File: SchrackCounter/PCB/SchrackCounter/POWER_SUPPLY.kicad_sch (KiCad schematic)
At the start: 4 parts, among them J1 Conn_01x02_Pin

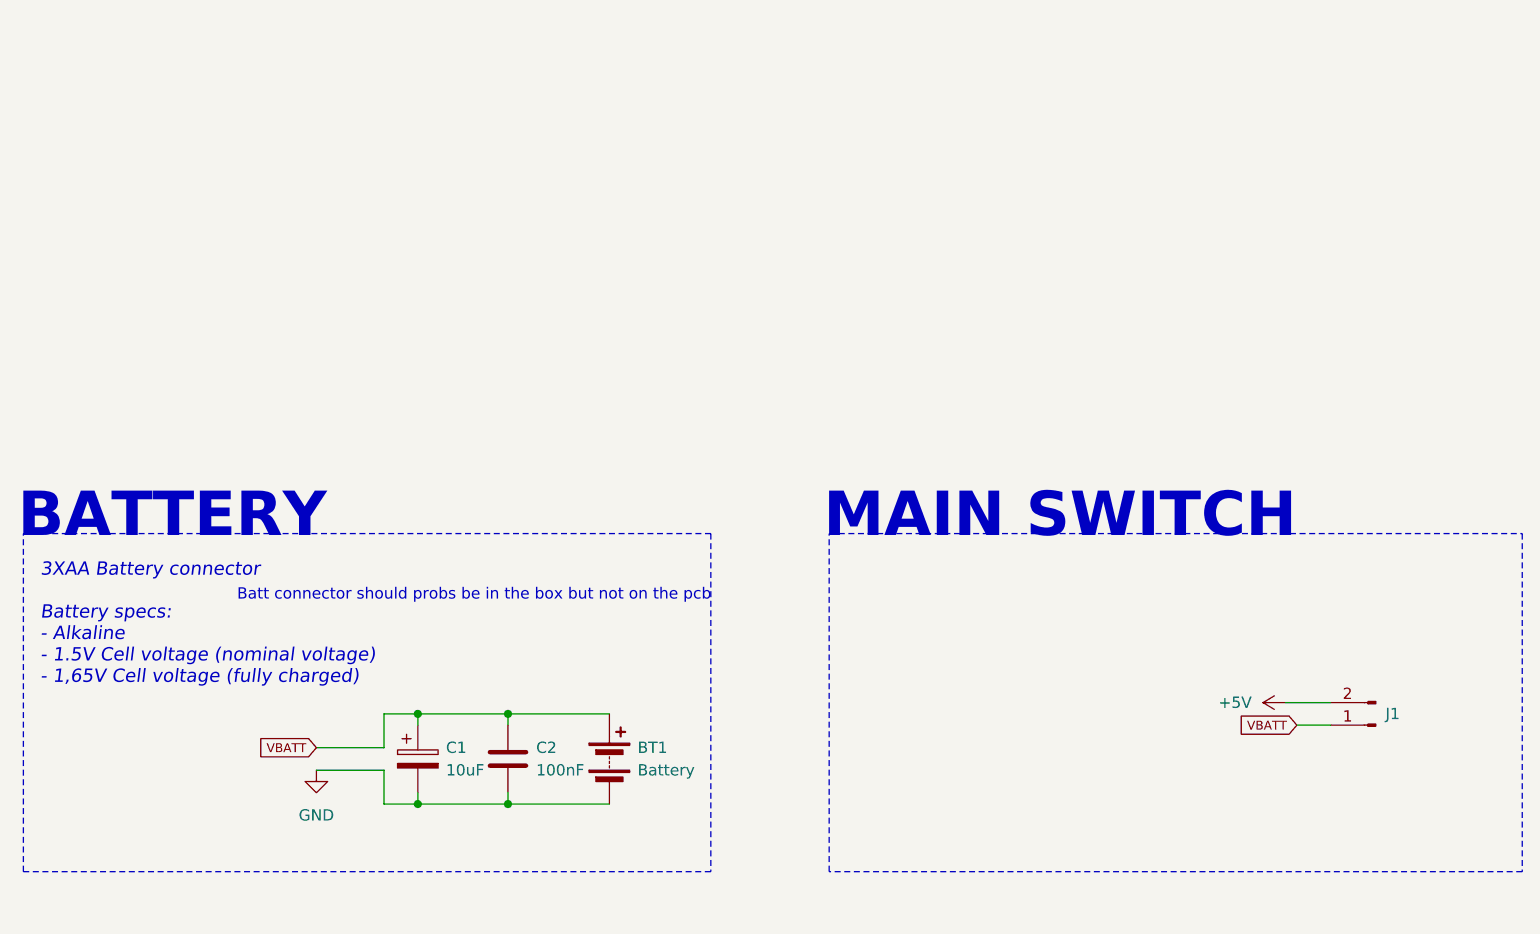
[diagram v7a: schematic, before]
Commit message: Schematic and PCB update
LDO Regulator, and some layout update
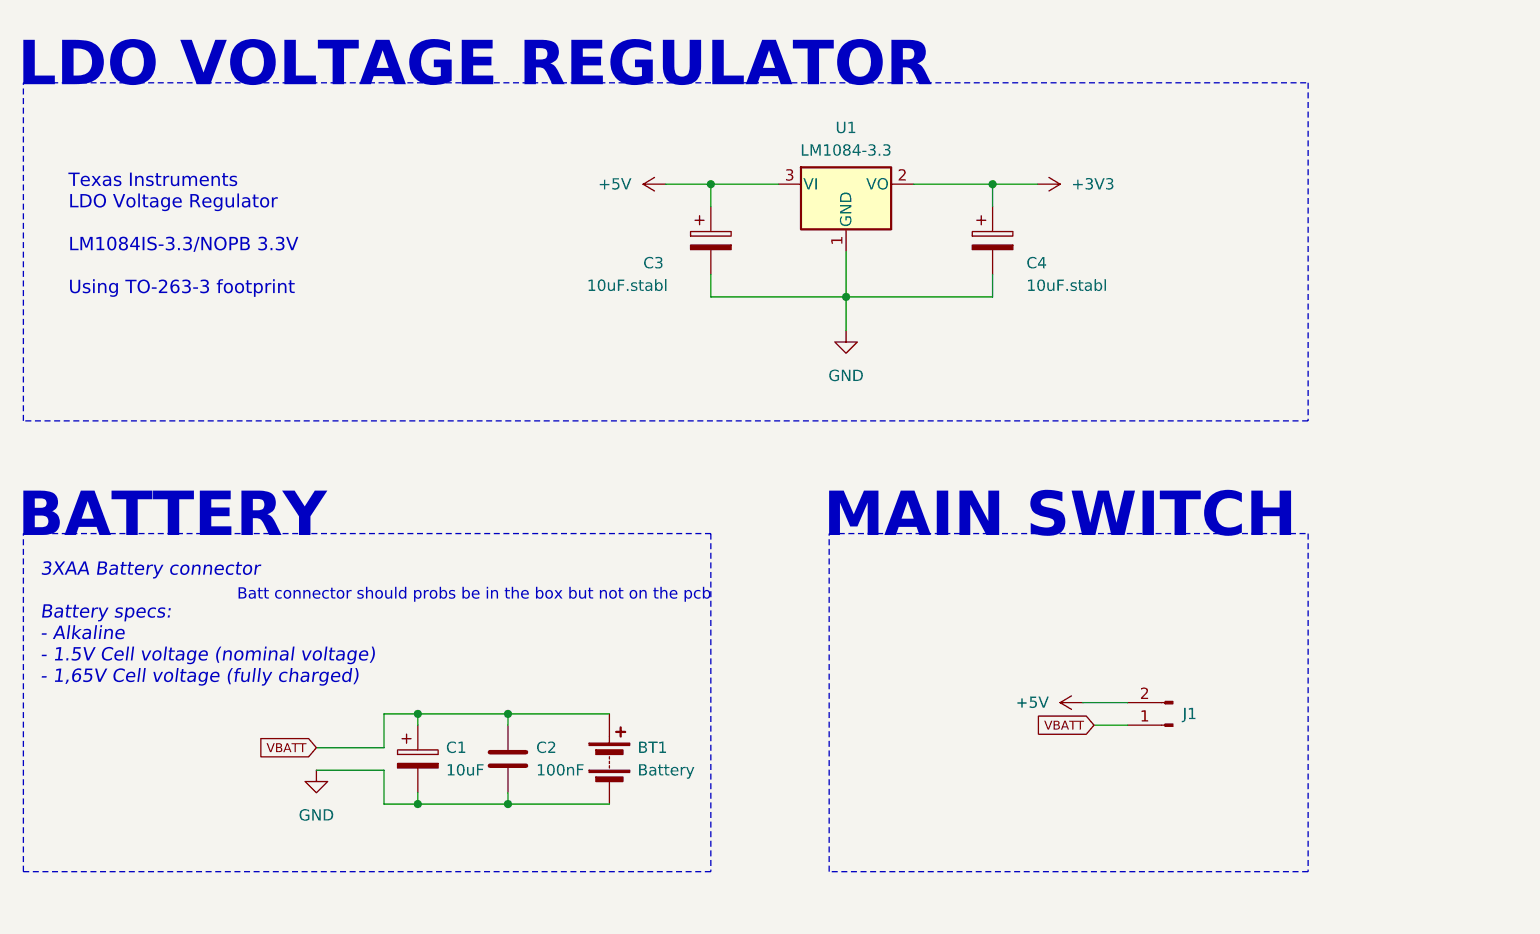
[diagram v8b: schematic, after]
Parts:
- added C3, C4: 10uF.stabl, Capacitor_Tantalum_SMD:CP_EIA-3216-18_Kemet-A_Pad1.58x1.35mm_HandSolder, symbol Device:C_Polarized
- added U1: LM1084-3.3, Package_TO_SOT_SMD:TO-263-3_TabPin2, symbol Regulator_Linear:LM1084-3.3
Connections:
- net +5V: now also C3.1, U1.3 (VI)
- net GND: now also C3.2, C4.2, U1.1 (GND)
- new net +3V3: C4.1, U1.2 (VO)
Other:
- note added: "LDO VOLTAGE REGULATOR"
- note added: "Texas Instruments LDO Voltage Regulator LM1084IS-3.3/NOPB 3.3V Using TO-263-3 footprint"
- moved on the sheet: J1
